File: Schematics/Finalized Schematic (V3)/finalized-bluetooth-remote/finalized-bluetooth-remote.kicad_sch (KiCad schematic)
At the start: 33 parts, among them J1 Conn_01x02, SW1 SW_SPDT, SW2 SW_Push, SW3 SW_Push, SW4 SW_Push, SW5 SW_Push, SW6 SW_SPDT, U1 XIAO ESP32C3, U2 OPA340P

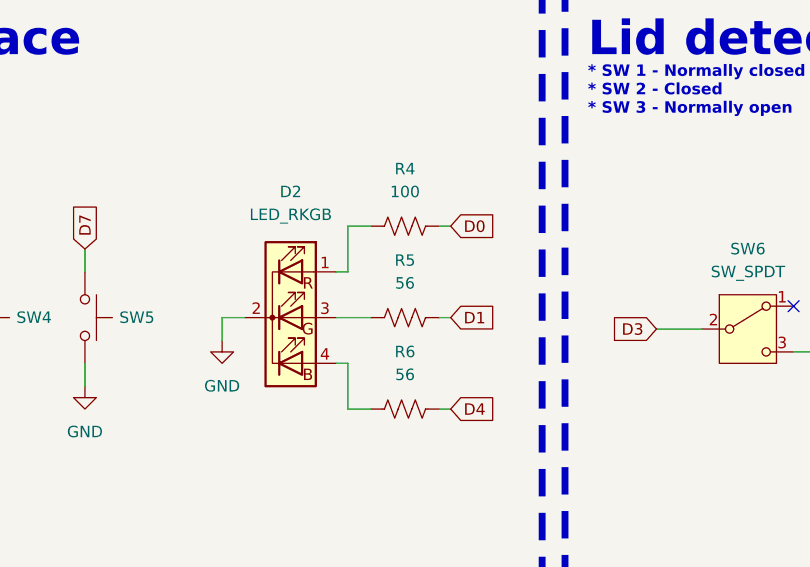
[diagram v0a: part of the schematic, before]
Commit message: Update resistors for LED
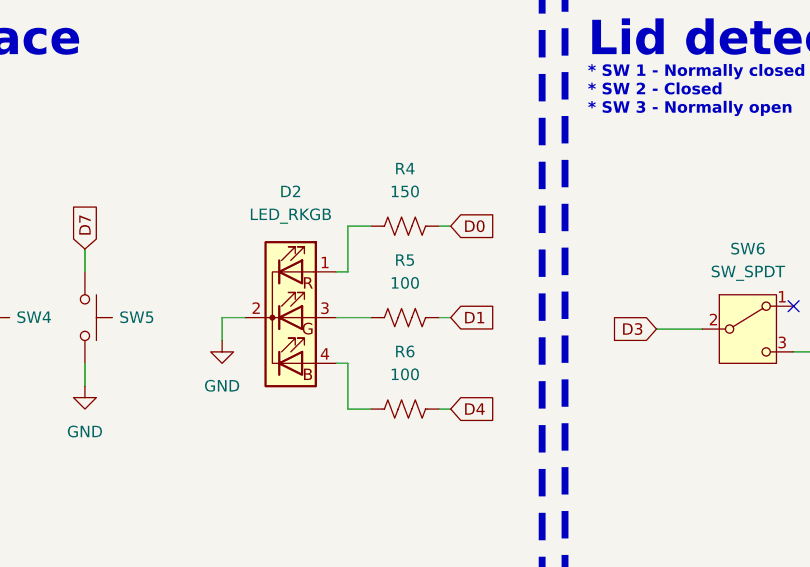
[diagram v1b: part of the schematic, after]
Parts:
- R4: value 100 -> 150
- R5, R6: value 56 -> 100
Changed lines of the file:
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@@
 			)
 		)
-		(property "Value" "56"
+		(property "Value" "100"
 			(at 226.06 57.15 90)
 			(effects
@@
 			)
 		)
-		(property "Value" "100"
+		(property "Value" "150"
 			(at 226.06 36.83 90)
 			(effects
@@
 			)
 		)
-		(property "Value" "56"
+		(property "Value" "100"
 			(at 226.06 46.99 90)
 			(effects
